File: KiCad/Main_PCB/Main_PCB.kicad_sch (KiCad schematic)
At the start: 11 parts, among them U1 ESP32-PICO-D4, U2 CP2102N-Axx-xQFN28

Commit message: Schematic Progress
-Added bounding Boxes
-Some USB-UART Stuff from ESP schematic
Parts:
- added J2: USB_C_Receptacle_USB2.0_14P, symbol Connector:USB_C_Receptacle_USB2.0_14P
- added Q1, Q2: S8050, Package_TO_SOT_THT:TO-92_Inline, symbol Transistor_BJT:S8050
- added R15, R16: 1K, symbol Device:R_US
- added R19, R20: 10K, symbol Device:R_US
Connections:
- net IO0: now reaches U1.23 (IO0)
- net IO0: now also Q2.3 (C)
- net RTS: now reaches U2.24 (~{RTS})
- net RTS: now also Q1.1 (E), R20.2
- net DTR: now reaches U2.28 (~{DTR})
- net DTR: now also Q2.1 (E), R19.2
- net U0RXD renamed RXD
- net RXD: now also R15.1; no longer U1.40 (U0RXD)
- net U0TXD renamed TXD
- net TXD: now also R16.1; no longer U1.41 (U0TXD)
- new net: J2.A1 (GND), J2.A12 (GND), J2.B1 (GND), J2.B12 (GND)
- new net: J2.A4 (VBUS), J2.A9 (VBUS), J2.B4 (VBUS), J2.B9 (VBUS)
- new net: Q1.2 (B), R19.1
- new net: Q2.2 (B), R20.1
- new net EN: Q1.3 (C)
- new net RXD0: R16.2, U1.40 (U0RXD)
- new net TXD0: R15.2, U1.41 (U0TXD)
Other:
- note added: "Battery Charging & Power Supply"
- note added: "USB-C 5V&USB-UART"
- moved on the sheet: C1, C15, C19, C2, C3, E1, L1, R1, R2, U1, U2

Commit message: push
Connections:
- net GNDREF: now also J2.A1 (GND), J2.A12 (GND), J2.B1 (GND), J2.B12 (GND)
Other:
- moved on the sheet: J2
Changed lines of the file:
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@@
+	(wire
+		(pts
+			(xy 106.68 208.28) (xy 106.68 212.09)
+		)
+		(stroke
+			(width 0)
+			(type default)
+		)
+	)
 	(wire
 		(pts
@@
 			)
 			(justify right bottom)
+		)
+	)
+	(symbol
+		(lib_id "power:GNDREF")
+		(at 106.68 212.09 0)
+		(unit 1)
+		(exclude_from_sim no)
+		(in_bom yes)
+		(on_board yes)
+		(dnp no)
+		(fields_autoplaced yes)
+		(property "Reference" "#PWR012"
+			(at 106.68 218.44 0)
+			(effects
+				(font
+					(size 1.27 1.27)
+				)
+				(hide yes)
+			)
+		)
+		(property "Value" "GNDREF"
+			(at 106.68 217.17 0)
+			(effects
+				(font
+					(size 1.27 1.27)
+				)
+			)
+		)
+		(property "Footprint" ""
+			(at 106.68 212.09 0)
+			(effects
+				(font
+					(size 1.27 1.27)
+				)
+				(hide yes)
+			)
+		)
+		(property "Datasheet" ""
+			(at 106.68 212.09 0)
+			(effects
+				(font
+					(size 1.27 1.27)
+				)
+				(hide yes)
+			)
+		)
+		(property "Description" "Power symbol creates a global label with name \"GNDREF\" , reference supply ground"
+			(at 106.68 212.09 0)
+			(effects
+				(font
+					(size 1.27 1.27)
+				)
+				(hide yes)
+			)
+		)
+		(pin "1"
+		)
+		(instances
+			(project "Main_PCB"
+				(path "/a8c606a5-861f-4fc4-bc4f-8db124604f29"
+					(reference "#PWR012")
+					(unit 1)
+				)
+			)
 		)
 	)
@@
 	(symbol
 		(lib_id "Connector:USB_C_Receptacle_USB2.0_14P")
-		(at 137.16 185.42 0)
+		(at 106.68 185.42 0)
 		(unit 1)
 		(exclude_from_sim no)
@@
 		(fields_autoplaced yes)
 		(property "Reference" "J2"
-			(at 137.16 162.56 0)
+			(at 106.68 162.56 0)
 			(effects
 				(font
@@
 		)
 		(property "Value" "USB_C_Receptacle_USB2.0_14P"
-			(at 137.16 165.1 0)
+			(at 106.68 165.1 0)
 			(effects
 				(font
@@
 		)
 		(property "Footprint" ""
-			(at 140.97 185.42 0)
+			(at 110.49 185.42 0)
 			(effects
 				(font
@@
 		)
 		(property "Datasheet" "https://www.usb.org/sites/default/files/documents/usb_type-c.zip"
-			(at 140.97 185.42 0)
+			(at 110.49 185.42 0)
 			(effects
 				(font
@@
 		)
 		(property "Description" "USB 2.0-only 14P Type-C Receptacle connector"
-			(at 137.16 185.42 0)
-			(effects
-				(font
+			(at 106.68 185.42 0)
+			(effects
+				(font

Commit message: Updated PCB
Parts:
- added C12, C6, C7: 0.1uF, symbol Device:C
- added D2: BAT760-7, symbol Device:D_Schottky
- added D3, D4, D5: ESD5D5.0CT1G, Diode_SMD:D_SOD-923, symbol Diode:ESD9B3.3ST5G
- added R24: 22.1K, symbol Device:R_US
- added R25: 10K, symbol Device:R_US
- added R26: 47.5K, symbol Device:R_US
- added R27: 2K, symbol Device:R_US
- added SW1, SW2: ~, symbol Switch:SW_Push
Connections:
- net +3.3V is gone; now on net VDD33: C15.1, C2.1, R1.1, R2.1, U1.1 (VDDA), U1.19 (VDD3P3_RTC), U1.3 (VDDA3P3), U1.37 (VDD3P3_CPU), U1.4 (VDDA3P3), U1.43 (VDDA), U1.46 (VDDA)
- net GNDREF is gone; now on net GND: C15.2, C19.2, C2.2, C3.2, E1.1, J2.A1 (GND), J2.A12 (GND), J2.B1 (GND), J2.B12 (GND), L1.2, U1.49 (GND)
- net EN: now also C7.1, SW2.2
- net IO0: now also C6.1, SW1.2
- net at U2.11 (~{SUSPEND}): now also R25.1
- net CTS: now reaches U2.23 (~{CTS})
- net GND: now reaches U2.29 (GND), U2.3 (GND)
- net GND: now also C12.2, C6.2, C7.2, D3.2 (A2), D4.2 (A2), D5.2 (A2), R25.2, R26.2, SW1.1, SW2.1
- net USB_DP: now reaches U2.4 (D+)
- net USB_DP: now also J2.A6 (D+), D4.1 (A1)
- net USB_DN: now reaches U2.5 (D-)
- net USB_DN: now also J2.A7 (D-), D3.1 (A1)
- net VDD33: now reaches U2.6 (VDD)
- net VDD33: now also U2.7 (VREGIN), C12.1, R27.1
- net at U2.8 (VBUS): now also R24.2, R26.1
- net at U2.9 (~{RST}): now also R27.2
- net at J2.A4 (VBUS), J2.A9 (VBUS), J2.B4 (VBUS)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: now also D2.2 (A), D5.1 (A1)
- new net EXT_5V: D2.1 (K), R24.1
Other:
- note added: "USB-C 5V & USB-UART"
- note removed: "USB-C 5V&USB-UART"
- moved on the sheet: J2, Q1, Q2, R15, R16, R19, R20, U2

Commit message: Added pump charge circuit
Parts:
- added BT1: LiPo, symbol Device:Battery_Cell
- added C2, C4: 10uF, symbol Device:C
- added C5, C9: 10uF, Adafruit AP6302:0805-NO, symbol Adafruit AP6302-eagle-import:CAP_CERAMIC0805-NOOUTLINE
- added C8: 1uF, Adafruit AP6302:0805-NO, symbol Adafruit AP6302-eagle-import:CAP_CERAMIC0805-NOOUTLINE
- added IC1: AP3602, Adafruit AP6302:SOT23-6, symbol Adafruit AP6302-eagle-import:AP3602
- added R3: 100K, Adafruit AP6302:0805-NO, symbol Adafruit AP6302-eagle-import:RESISTOR0805_NOOUTLINE
- added SW3: Main Power, symbol Switch:SW_SPST
- added U3: AMS1117, Package_TO_SOT_SMD:SOT-223-3_TabPin2, symbol Regulator_Linear:AMS1117
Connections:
- net EXT_5V: now also BT1.1 (+)
- net GND: now also C2.2, C4.2, C5.2, C9.2, IC1.2 (GND), U3.1 (ADJ)
- net VDD33: now also C2.1, U3.2 (VO)
- new net: C8.1, IC1.4 (C-)
- new net: C8.2, IC1.6 (C+)
- new net: BT1.2 (-), SW3.1 (A)
- new net 5.0V: C9.1, IC1.1 (5VO)
- new net VDD3.7_Bat: C4.1, U3.3 (VI)
- new net VIN: C5.1, IC1.5 (VIN), R3.1
- new net ~{SHDN}: IC1.3 (~{SHDN}), R3.2
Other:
- moved on the sheet: C6, C7, D2, D3, D4, D5, J2, Q1, Q2, R15, R16, R19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

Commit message: Added charging circuit
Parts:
- added C10, C11: 10uF, Adafruit AP6302:0805-NO, symbol Adafruit AP6302-eagle-import:CAP_CERAMIC0805-NOOUTLINE
- added GREEN: LED2, symbol Device:LED
- added R4: 2K, symbol Device:R_US
- added R5, R6: 10K, symbol Device:R_US
- added RED: LED1, symbol Device:LED
- added U4: MCP73831-2-OT, Package_TO_SOT_SMD:SOT-23-5, symbol Battery_Management:MCP73831-2-OT
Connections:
- net GND: now also C10.1, C11.2, GREEN.1 (K), R6.2, U4.2 (V_{SS})
- net VDD3.7_Bat: now also C11.1, U4.3 (V_{BAT})
- new net: R4.1, R5.1, U4.1 (STAT)
- new net: R4.2, RED.1 (K)
- new net: GREEN.2 (A), R5.2
- new net: R6.1, U4.5 (PROG)
- new net USB_5V: C10.2, RED.2 (A), U4.4 (V_{DD})
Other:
- note added: "10K = 100mA"
- moved on the sheet: R3

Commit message: Finished charging circuit
Need someone to double check and make sure nothing else needs added before work on the pcb design starts
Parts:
- removed BT1: LiPo, symbol Device:Battery_Cell
- added BT2: LiPo, symbol Device:Battery_Cell
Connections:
- net GND: now also BT2.2 (-)
- net USB_5V: now also D2.1 (K)
- net VDD3.7_Bat: now also SW3.2 (B); no longer C11.1, U4.3 (V_{BAT})
- net VDD33: no longer C12.1, C15.1, C2.1, C2.1, R1.1, R2.1, R27.1, U1.1 (VDDA), U1.19 (VDD3P3_RTC), U1.3 (VDDA3P3), U1.4 (VDDA3P3), U2.6 (VDD), U2.7 (VREGIN), U3.2 (VO)
- net at SW3.1 (A): now also C11.1, U4.3 (V_{BAT}), BT2.1 (+)
- net 5.0V renamed VDD5
- net VDD5: now also R24.1
- removed net EXT_5V: D2.1 (K), R24.1
- net VIN renamed VDD3.3
- net VDD3.3: now also C12.1, C15.1, C2.1, C2.1, R1.1, R2.1, R27.1, U1.1 (VDDA), U1.19 (VDD3P3_RTC), U1.3 (VDDA3P3), U1.4 (VDDA3P3), U2.6 (VDD), U2.7 (VREGIN), U3.2 (VO); no longer R3.1
- new net 3.3V: R3.1
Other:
- note added: "3.3V Regulator"
- note added: "Charger Circuit"
- note added: "Pump Charger"
- moved on the sheet: C10, C11, C2, C4, C5, C8, C9, GREEN, IC1, R3, R4, R5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

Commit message: Cleaned up for Milestone #2
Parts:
- BT1: renamed from BT2; footprint (none) -> TestPoint:TestPoint_2Pads_Pitch2.54mm_Drill0.8mm
- C1: renamed from C19; footprint (none) -> Capacitor_SMD:C_1206_3216Metric
- C10: renamed from C8; footprint Adafruit AP6302:0805-NO -> Capacitor_SMD:C_1206_3216Metric
- C11: renamed from C4; footprint (none) -> Capacitor_SMD:C_1206_3216Metric
- C12: renamed from C10; footprint Adafruit AP6302:0805-NO -> Capacitor_SMD:C_1206_3216Metric
- C13: renamed from C11; footprint Adafruit AP6302:0805-NO -> Capacitor_SMD:C_1206_3216Metric
- C14, C5: renamed from C2; footprint (none) -> Capacitor_SMD:C_1206_3216Metric
- C15: renamed from C9; footprint Adafruit AP6302:0805-NO -> Capacitor_SMD:C_1206_3216Metric
- C2: renamed from C15; footprint (none) -> Capacitor_SMD:C_1206_3216Metric
- C3: footprint (none) -> Capacitor_SMD:C_1206_3216Metric
- C4: renamed from C1; footprint (none) -> Capacitor_SMD:C_1206_3216Metric
- C6: renamed from C12; footprint (none) -> Capacitor_SMD:C_1206_3216Metric
- C7: renamed from C6; footprint (none) -> Capacitor_SMD:C_1206_3216Metric
- C8: renamed from C7; footprint (none) -> Capacitor_SMD:C_1206_3216Metric
- C9: renamed from C5; footprint Adafruit AP6302:0805-NO -> Capacitor_SMD:C_1206_3216Metric
- D3: renamed from D2; footprint (none) -> Diode_SMD:D_SOD-923
- E1: footprint PRO-OB-440:XDCR_PRO-OB-440 -> RF_Antenna:Abracon_PRO-OB-440
- GREEN1: renamed from GREEN; footprint (none) -> LED_THT:LED_D3.0mm
- J1: renamed from J2; footprint (none) -> Connector_USB:USB_C_Receptacle_Amphenol_12401548E4-2A
- L1: footprint (none) -> Inductor_SMD:L_1206_3216Metric
- R1: renamed from R24; footprint (none) -> Resistor_SMD:R_1206_3216Metric
- R10: renamed from R16; footprint (none) -> Resistor_SMD:R_1206_3216Metric
- R11: renamed from R6; footprint (none) -> Resistor_SMD:R_1206_3216Metric
- R12: renamed from R3; footprint Adafruit AP6302:0805-NO -> Resistor_SMD:R_1206_3216Metric
- R13: renamed from R5; footprint (none) -> Resistor_SMD:R_1206_3216Metric
- R14: renamed from R4; footprint (none) -> Resistor_SMD:R_1206_3216Metric
- R2: renamed from R26; footprint (none) -> Resistor_SMD:R_1206_3216Metric
- R3: renamed from R2; footprint (none) -> Resistor_SMD:R_1206_3216Metric
- R4: renamed from R27; footprint (none) -> Resistor_SMD:R_1206_3216Metric
- R5: renamed from R25; footprint (none) -> Resistor_SMD:R_1206_3216Metric
- R6: renamed from R1; footprint (none) -> Resistor_SMD:R_1206_3216Metric
- R7: renamed from R19; footprint (none) -> Resistor_SMD:R_1206_3216Metric
- R8: renamed from R20; footprint (none) -> Resistor_SMD:R_1206_3216Metric
- R9: renamed from R15; footprint (none) -> Resistor_SMD:R_1206_3216Metric
- RED1: renamed from RED; footprint (none) -> LED_THT:LED_D3.0mm
- U2: renamed from U1; footprint ESP32-PICO-D4_EXP -> (none)
- renumbered D5 to D1, D3 to D2, U2 to U1, U4 to U3, U3 to U4
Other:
- note added: "Auto Boot Mode"
- note added: "ESP32 Pico D4"
- note added: "Enable Switch"
- note added: "Reset Switch"
- note added: "USB-C Receptacle"
- note added: "USB-UART Bridge"
- moved on the sheet: BT1, C1, C10, C11, C12, C13, C15, C2, C3, C4, C5, C6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

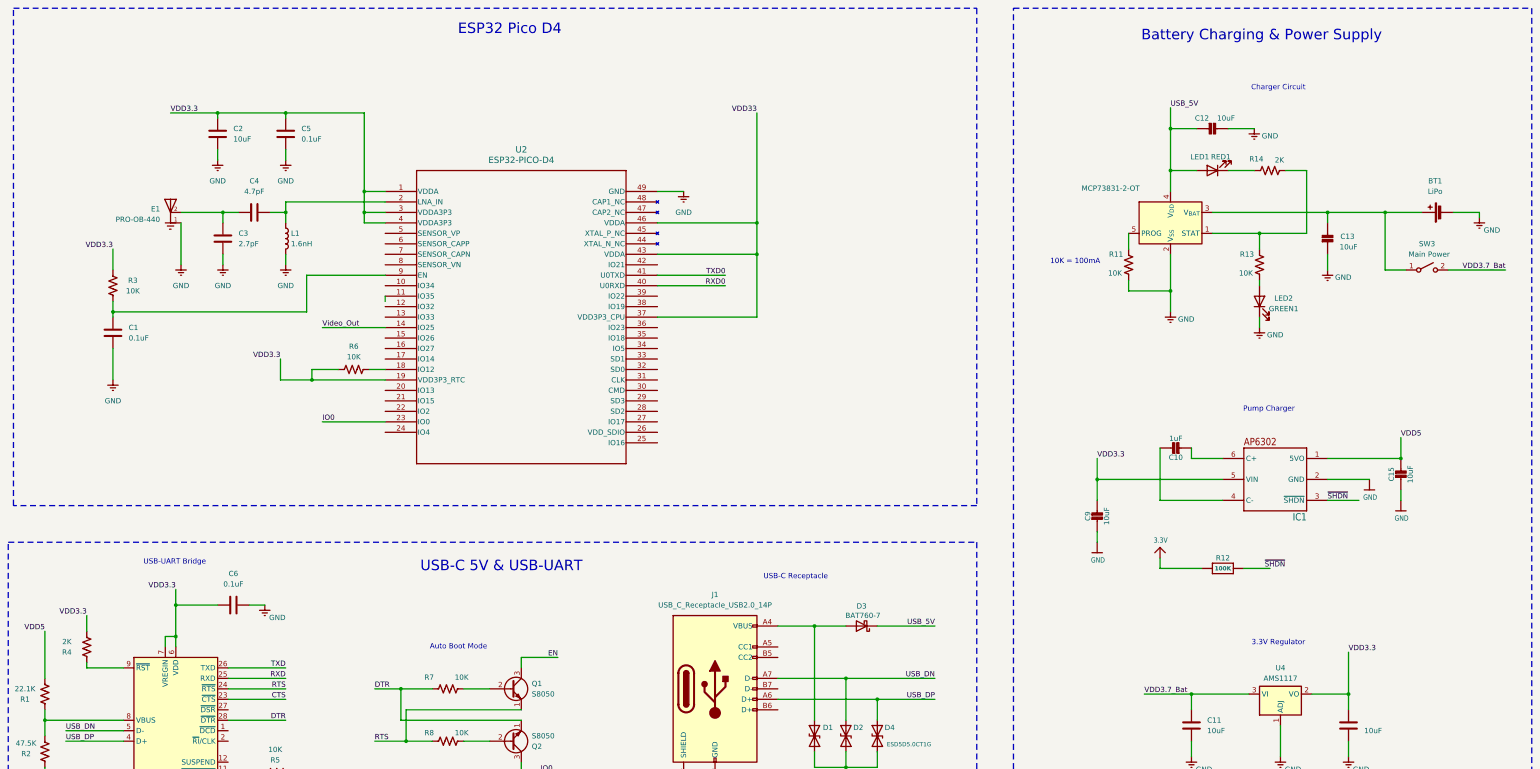
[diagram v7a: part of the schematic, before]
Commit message: Fixed ERC errors and added power inputs
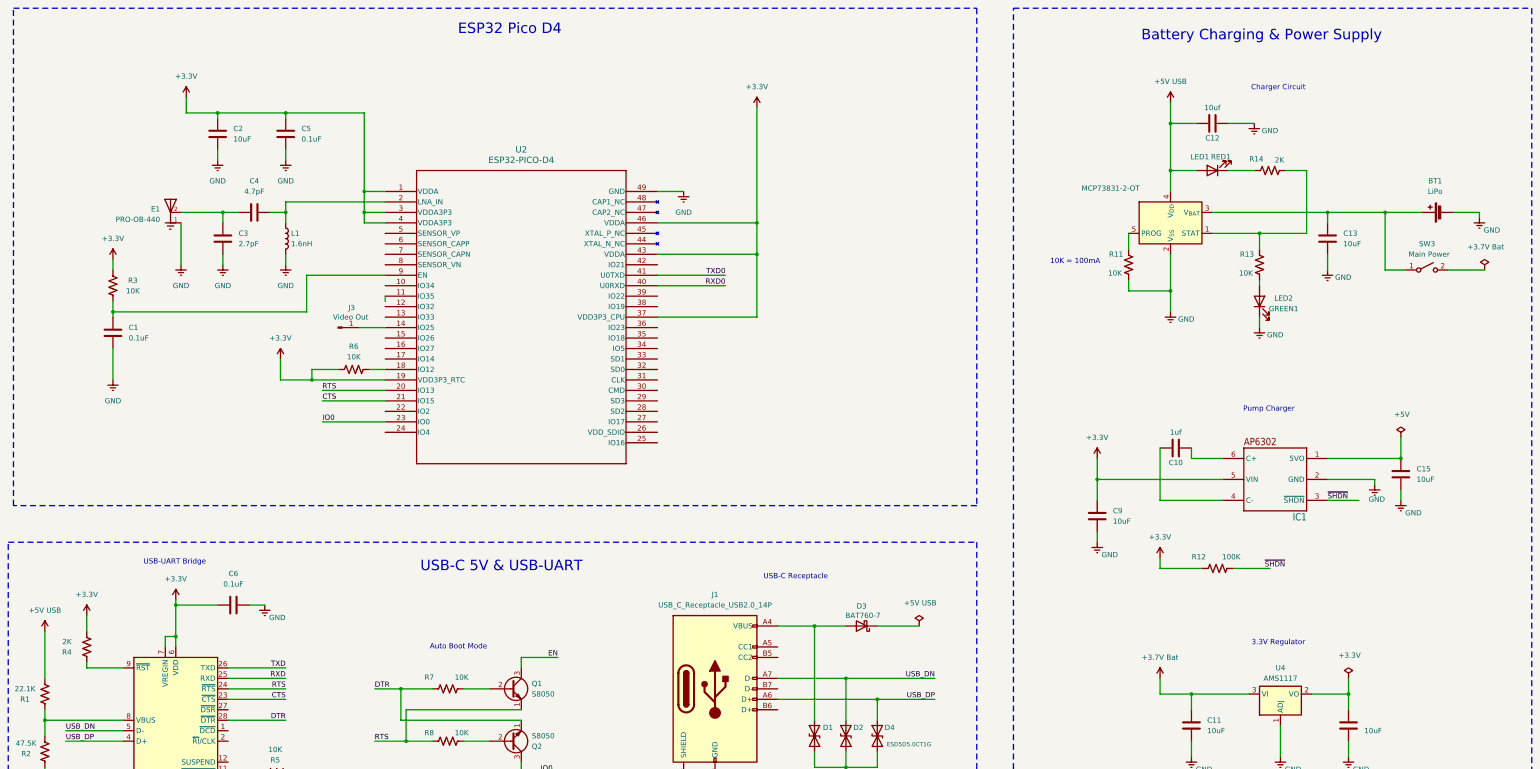
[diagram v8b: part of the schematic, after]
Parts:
- removed C10: 1uF, Capacitor_SMD:C_1206_3216Metric, symbol Adafruit AP6302-eagle-import:CAP_CERAMIC0805-NOOUTLINE
- removed C12, C13, C15, C9: 10uF, Capacitor_SMD:C_1206_3216Metric, symbol Adafruit AP6302-eagle-import:CAP_CERAMIC0805-NOOUTLINE
- removed R12: 100K, Resistor_SMD:R_1206_3216Metric, symbol Adafruit AP6302-eagle-import:RESISTOR0805_NOOUTLINE
- added C10: 1uf, Capacitor_SMD:C_1206_3216Metric, symbol Device:C
- added C12: 10uf, Capacitor_SMD:C_1206_3216Metric, symbol Device:C
- added C13, C15, C9: 10uF, Capacitor_SMD:C_1206_3216Metric, symbol Device:C
- added J3: Video Out, Connector_Wire:SolderWire-0.1sqmm_1x01_D0.4mm_OD1mm, symbol Connector:Conn_01x01_Pin
- added R12: 100K, Resistor_SMD:R_1206_3216Metric, symbol Device:R_US
- BT1: footprint TestPoint:TestPoint_2Pads_Pitch2.54mm_Drill0.8mm -> Connector_Wire:SolderWire-0.1sqmm_1x01_D0.4mm_OD1mm
- IC1: footprint Adafruit AP6302:SOT23-6 -> Package_TO_SOT_SMD:SOT-23-6
- SW1, SW2: footprint (none) -> Button_Switch_SMD:SW_Push_SPST_NO_Alps_SKRK
- SW3: footprint (none) -> Button_Switch_SMD:SW_DIP_SPSTx01_Slide_6.7x4.1mm_W6.73mm_P2.54mm_LowProfile_JPin
- U2: footprint (none) -> ESP32 PICO D4:ESP32-PICO-D4_EXP
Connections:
- net VDD33 is gone; now on net +3.3V: U2.37 (VDD3P3_CPU), U2.43 (VDDA), U2.46 (VDDA)
- net CTS: now also U2.21 (IO15)
- net GND: now also C12.1, C13.2, C15.2, C9.2
- net RTS: now also U2.20 (IO13)
- net ~{SHDN}: now also R12.1
- net at BT1.1 (+), SW3.1 (A), U3.3 (V_{BAT}): now also C13.1
- net at IC1.4 (C-): now also C10.2
- net at IC1.6 (C+): now also C10.1
- net USB_5V renamed +5V USB
- net +5V USB: now also R1.1, C12.2; no longer D3.1 (K)
- net VDD3.3 renamed +3.3V
- net +3.3V: now also C9.1, R12.2; no longer C14.1, U4.2 (VO)
- net VDD3.7_Bat renamed +3.7V Bat
- net +3.7V Bat: no longer SW3.2 (B)
- net VDD5: no longer names the net of IC1.1 (5VO)
- net VDD5: now also C15.1; no longer R1.1
- net Video_Out: no longer names the net of U2.14 (IO25)
- net Video_Out: now also J3.1 (Pin_1)
- new net: C14.1, U4.2 (VO)
